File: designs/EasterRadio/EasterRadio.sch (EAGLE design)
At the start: 70 parts, among them IC1 MCP73832T-2ACI_OT, IC3 DMP1045U-7, IC6 ESP32-WROVER-B, J1 S2B-NSHSS-TB, J2 S2B-NSHSS-TB, J3 S2B-NSHSS-TB, J4 S2B-PH-SM4, J5 S2B-NSHSS-TB, J6 PJ-002AH-SMT-TR, Q1 2SC3838T146, Y1 32.768kHz crystal

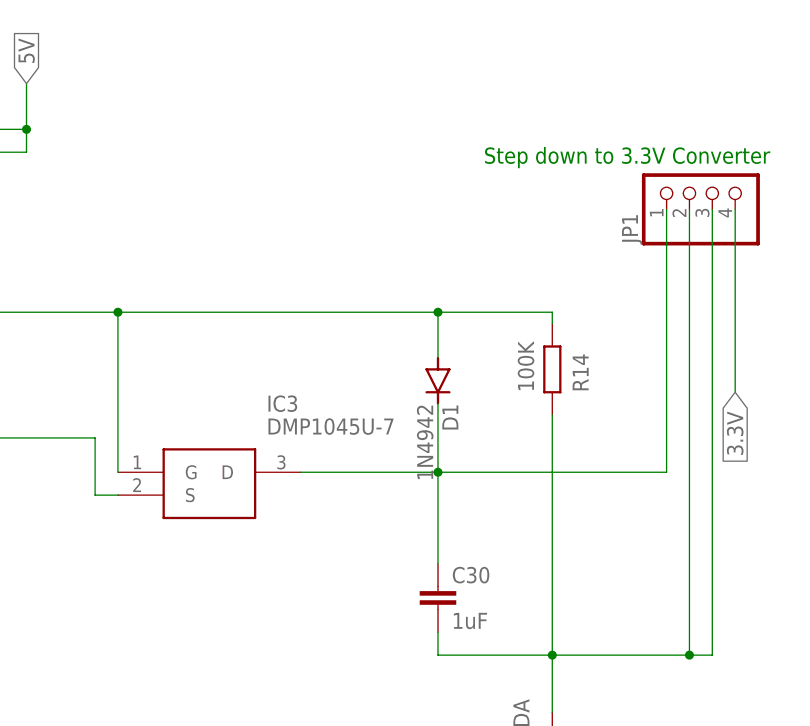
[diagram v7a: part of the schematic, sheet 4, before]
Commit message: changed to correct diode and designed power pcb
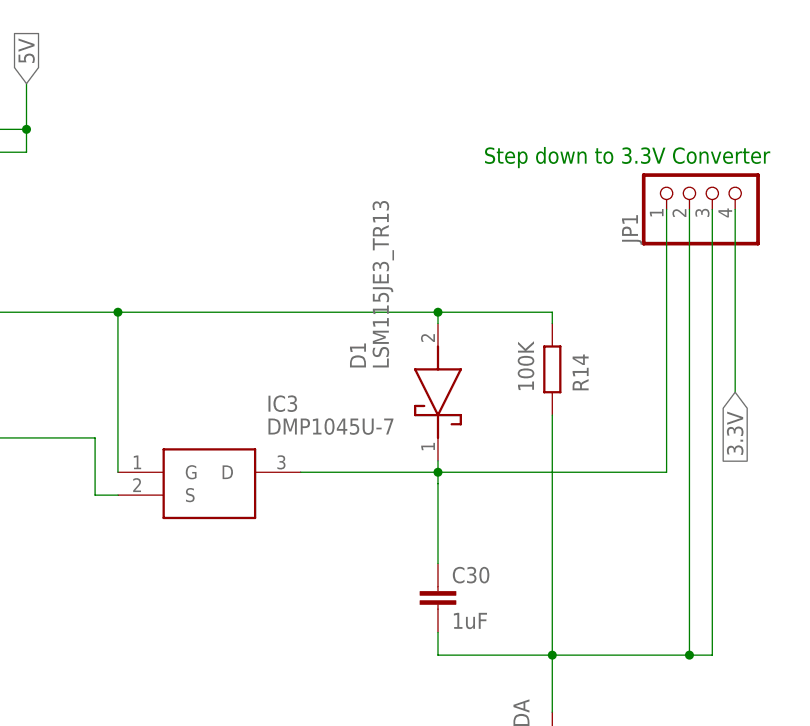
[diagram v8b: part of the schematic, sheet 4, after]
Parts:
- D1: value 1N4942 -> LSM115JE3_TR13; device diode:1N4942 -> CommonParts:LSM115JE3_TR13
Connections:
- net 12V: now also D1.K; no longer D1.C
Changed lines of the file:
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@@
 <part name="JP1" library="pinhead" library_urn="urn:adsk.eagle:library:325" deviceset="PINHD-1X4" device="" package3d_urn="urn:adsk.eagle:package:22407/2"/>
 <part name="IC3" library="MouserUseful" deviceset="DMP1045U-7" device=""/>
-<part name="D1" library="diode" library_urn="urn:adsk.eagle:library:210" deviceset="1N4942" device="" package3d_urn="urn:adsk.eagle:package:43336/1"/>
 <part name="R14" library="CommonParts" deviceset="R-EU_1206" device="R1206" package3d_urn="urn:adsk.eagle:package:23540/2" value="100K"/>
 <part name="GND9" library="supply1" library_urn="urn:adsk.eagle:library:371" deviceset="GNDA" device=""/>
 <part name="C30" library="CommonParts" deviceset="C-EU_805" device="C0805" package3d_urn="urn:adsk.eagle:package:23617/2" value="1uF"/>
+<part name="D1" library="CommonParts" deviceset="LSM115JE3_TR13" device=""/>
 </parts>
 <sheets>
@@
 <wire x1="116.84" y1="91.44" x2="165.1" y2="91.44" width="0.1524" layer="91"/>
 <wire x1="165.1" y1="91.44" x2="165.1" y2="99.06" width="0.1524" layer="91"/>
-<junction x="162.56" y="91.44"/>
 <pinref part="C17" gate="G$1" pin="2"/>
 <wire x1="165.1" y1="99.06" x2="170.18" y2="99.06" width="0.1524" layer="91"/>
@@
 <wire x1="116.84" y1="88.9" x2="165.1" y2="88.9" width="0.1524" layer="91"/>
 <wire x1="165.1" y1="88.9" x2="165.1" y2="81.28" width="0.1524" layer="91"/>
-<junction x="165.1" y="88.9"/>
 <wire x1="165.1" y1="81.28" x2="170.18" y2="81.28" width="0.1524" layer="91"/>
 <pinref part="C16" gate="G$1" pin="2"/>
@@
 <attribute name="VALUE" x="125.73" y="49.53" size="1.778" layer="96" align="center-left"/>
 </instance>
-<instance part="D1" gate="1" x="144.78" y="54.61" smashed="yes" rot="R270">
-<attribute name="NAME" x="145.2626" y="52.07" size="1.778" layer="95" rot="R270"/>
-<attribute name="VALUE" x="142.4686" y="52.07" size="1.778" layer="96" rot="R270"/>
-</instance>
 <instance part="R14" gate="G$1" x="157.48" y="55.88" smashed="yes" rot="R270">
 <attribute name="NAME" x="161.5186" y="53.34" size="1.778" layer="95" rot="R90"/>
@@
 <attribute name="NAME" x="146.304" y="32.131" size="1.778" layer="95"/>
 <attribute name="VALUE" x="146.304" y="27.051" size="1.778" layer="96"/>
+</instance>
+<instance part="D1" gate="G$1" x="144.78" y="43.18" smashed="yes" rot="R90">
+<attribute name="NAME" x="135.89" y="55.88" size="1.778" layer="95" rot="R90" align="center-left"/>
+<attribute name="VALUE" x="138.43" y="55.88" size="1.778" layer="96" rot="R90" align="center-left"/>
 </instance>
 </instances>
@@
 <pinref part="IC3" gate="G$1" pin="D"/>
 <wire x1="129.54" y1="44.45" x2="144.78" y2="44.45" width="0.1524" layer="91"/>
-<pinref part="D1" gate="1" pin="C"/>
-<wire x1="144.78" y1="44.45" x2="144.78" y2="52.07" width="0.1524" layer="91"/>
-<wire x1="144.78" y1="44.45" x2="144.78" y2="34.29" width="0.1524" layer="91"/>
+<wire x1="144.78" y1="44.45" x2="144.78" y2="43.18" width="0.1524" layer="91"/>
 <junction x="144.78" y="44.45"/>
+<wire x1="144.78" y1="43.18" x2="144.78" y2="34.29" width="0.1524" layer="91"/>
 <wire x1="170.18" y1="73.66" x2="170.18" y2="44.45" width="0.1524" layer="91"/>
 <wire x1="170.18" y1="44.45" x2="144.78" y2="44.45" width="0.1524" layer="91"/>
 <pinref part="C30" gate="G$1" pin="1"/>
+<pinref part="D1" gate="G$1" pin="K"/>
+<wire x1="144.78" y1="45.72" x2="144.78" y2="44.45" width="0.1524" layer="91"/>
 </segment>
 </net>
@@
 <wire x1="109.22" y1="44.45" x2="109.22" y2="62.23" width="0.1524" layer="91"/>
 <wire x1="109.22" y1="62.23" x2="144.78" y2="62.23" width="0.1524" layer="91"/>
-<wire x1="144.78" y1="62.23" x2="144.78" y2="57.15" width="0.1524" layer="91"/>
-<pinref part="D1" gate="1" pin="A"/>
+<wire x1="144.78" y1="62.23" x2="144.78" y2="60.96" width="0.1524" layer="91"/>
 <wire x1="144.78" y1="62.23" x2="157.48" y2="62.23" width="0.1524" layer="91"/>
 <junction x="144.78" y="62.23"/>
@@
 <junction x="17.78" y="38.1"/>
 <junction x="109.22" y="62.23"/>
+<pinref part="D1" gate="G$1" pin="A"/>
 </segment>
 <segment>
@@
 </sheet>
 </sheets>
+<errors>
+</errors>
 </schematic>
 </drawing>
